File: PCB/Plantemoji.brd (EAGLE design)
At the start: 66.8 x 71 mm, 34 parts, among them IC3 MEGA8-P, Q1 TIP120, Q2 TIP120

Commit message: Putting all the components on the board without routing for now
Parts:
- moved EXTRA_GPIO 253.5 mm to (-5.33, 86.4), turned to 90 degrees
- moved SI1145 199.7 mm to (-9.40, 41.4)
- moved R7 199.5 mm to (-7.37, 35.3)
- moved R6 198.7 mm to (-11.2, 51.8), turned to 90 degrees
- moved Q2 192.6 mm to (-18.0, 92.2), turned to 90 degrees
- moved WATER_LEVEL 191.2 mm to (-19.6, 41.4), turned to 180 degrees
- moved JP2_TX 186.4 mm to (21.1, 92.2)
- moved R1 182.6 mm to (-15.2, 51.8), turned to 90 degrees
- moved DS18B20 178.4 mm to (-28.2, 41.1)
- moved HW-390 170.1 mm to (-37.8, 41.1)
- moved HUMIDIFIER_OUT 152.1 mm to (-20.1, 33.8)
- moved JP2_RX 151.4 mm to (-30.5, 83.8)
- moved R2-0.25W 151.1 mm to (2.79, 79.2), turned to 270 degrees
- moved R3-0.25W 143.4 mm to (3.30, 65.3), turned to 90 degrees
- moved LCD_SCREEN 143.2 mm to (7.37, 96.8), turned to 180 degrees
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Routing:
- net +5V: track 77.3 -> 0.00 mm
- net RESET: track 44.7 -> 0.00 mm
- net N$14: track 12.3 -> 0.00 mm
- net +12V: track 4.57 -> 0.00 mm
- net N$1: track 2.03 -> 0.00 mm

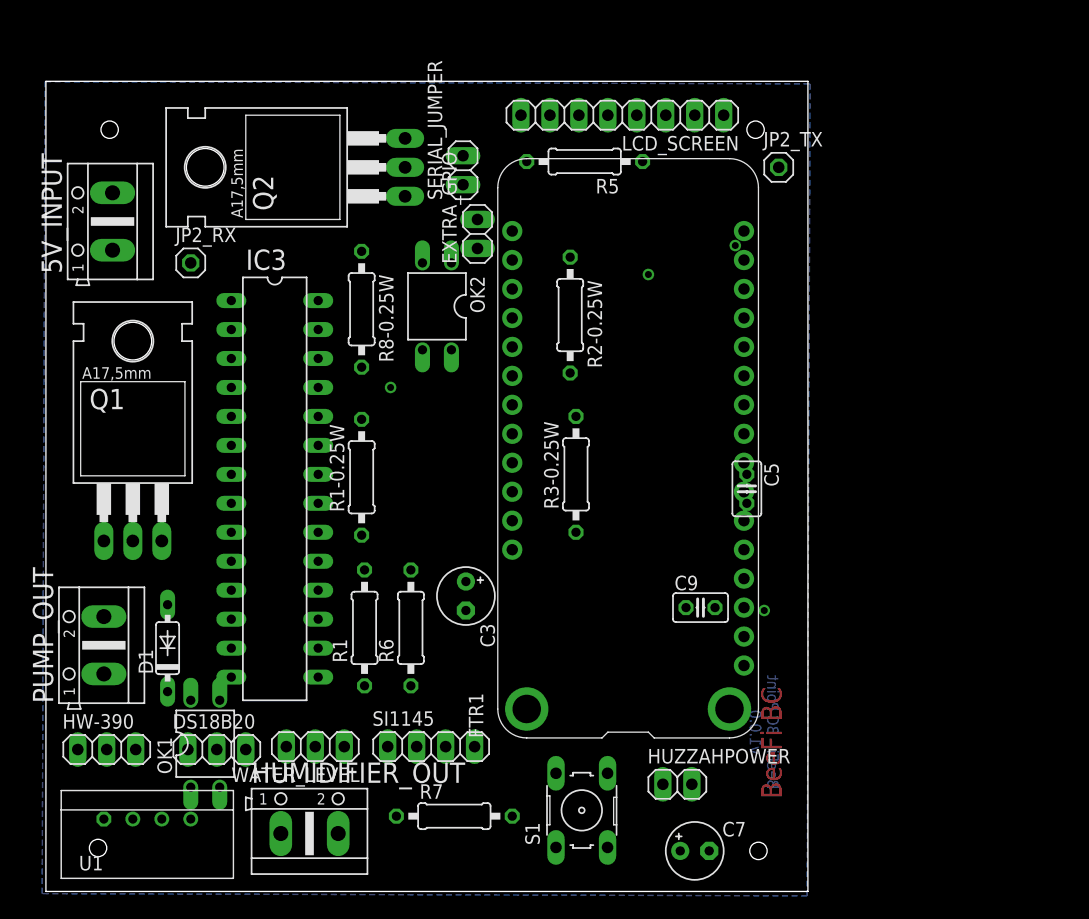
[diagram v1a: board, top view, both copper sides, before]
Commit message: Finish wiring the PCB
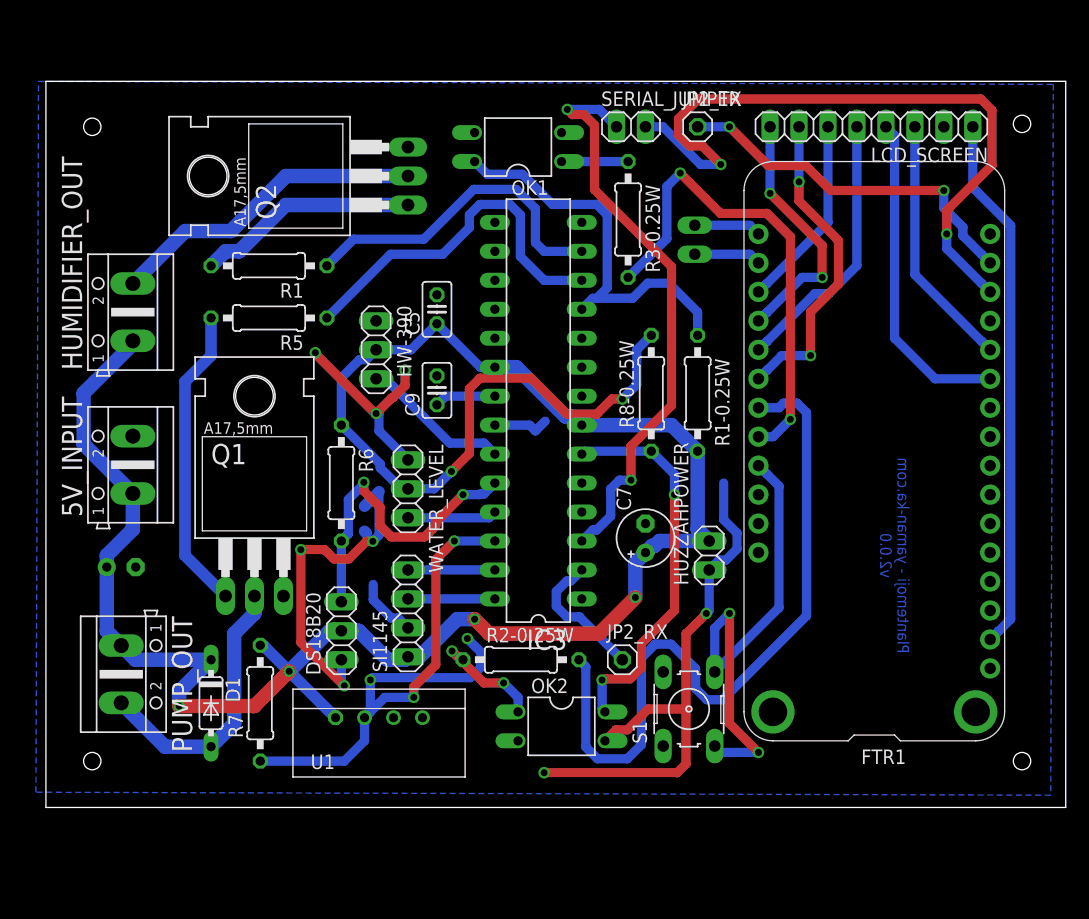
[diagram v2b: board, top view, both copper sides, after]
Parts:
- moved OK1 59.1 mm to (-1.78, 94.0), turned to 90 degrees
- moved JP2_RX 51.4 mm to (7.37, 49.0)
- moved HUMIDIFIER_OUT 48.3 mm to (-35.6, 79.5), turned to 90 degrees
- moved HW-390 42.3 mm to (-14.2, 76.2), turned to 270 degrees
- moved OK2 38.4 mm to (2.03, 43.2), turned to 270 degrees
- moved R1 32.8 mm to (-23.6, 83.6), turned to 180 degrees
- moved C5 31.4 mm to (-8.89, 79.8), turned to 90 degrees
- moved R5 30.9 mm to (-23.6, 79.0)
- moved R2-0.25W 30.5 mm to (-1.52, 49.0), turned to 0 degrees
- moved R1-0.25W 30.4 mm to (14.0, 72.4), turned to 270 degrees
- moved C3 30.3 mm to (-36.6, 57.1), flipped to the bottom, turned to 180 degrees
- moved C9 30.0 mm to (-8.89, 72.6), turned to 90 degrees
- moved C7 27.8 mm to (9.40, 59.7), turned to 90 degrees
- moved R8-0.25W 26.4 mm to (9.91, 72.4), turned to 90 degrees
- moved IC3 24.1 mm to (0.00, 70.9), turned to 90 degrees
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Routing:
- net +5V: track 0.00 -> 205.3 mm, vias 1 -> 6
- net GND: track 0.00 -> 106.4 mm, vias 0 -> 8
- net N$13: track 0.00 -> 65.0 mm
- net N$4: track 0.00 -> 61.9 mm, vias 0 -> 2
- net N$28: track 0.00 -> 52.4 mm, vias 0 -> 4
- net N$3: track 0.00 -> 51.2 mm, vias 0 -> 2
- net 3V3: track 0.00 -> 47.1 mm
- net N$2: track 0.00 -> 44.2 mm, vias 0 -> 2
- net N$16: track 0.00 -> 42.4 mm, vias 0 -> 2
- net N$1: track 0.00 -> 35.5 mm
- net N$11: track 0.00 -> 34.0 mm, vias 0 -> 2
- net N$21: track 0.00 -> 32.0 mm
- net N$18: track 0.00 -> 31.9 mm, vias 0 -> 2
- net N$24: track 0.00 -> 29.1 mm
- net N$6: track 0.00 -> 28.7 mm
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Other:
- board size 66.8 x 71 mm -> 89.4 x 63.7 mm
- board text added: "Plantemoji - yaman-ka.com v2.0.0"
- board text removed: "BeeFi - BC Point v1.0.0"
- board text removed: "BeeFi BC"

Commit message: Final touches before gerber files export
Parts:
- moved JP2_RX 0.72 mm to (6.86, 49.5)
- moved R2-0.25W 0.36 mm to (-1.78, 49.3)
- moved SERIAL_JUMPER 0.25 mm to (8.38, 95.8)
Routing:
- net N$4: track 61.9 -> 36.7 mm
- net +5V: track 205.3 -> 223.5 mm
- net N$28: track 52.4 -> 35.7 mm, vias 4 -> 2
- net N$3: track 51.2 -> 54.1 mm
- net GND: track 106.4 -> 109.2 mm, vias 8 -> 9
- net N$13: track 65.0 -> 67.4 mm
- net N$12: track 10.1 -> 7.82 mm, vias 2 -> 0
- net N$11: track 34.0 -> 36.2 mm
- net N$17: track 12.1 -> 11.3 mm
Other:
- board text added: "Plantemoji - yaman-ka.com CASA - UCL v2.0.0"
- board text removed: "Plantemoji - yaman-ka.com v2.0.0"

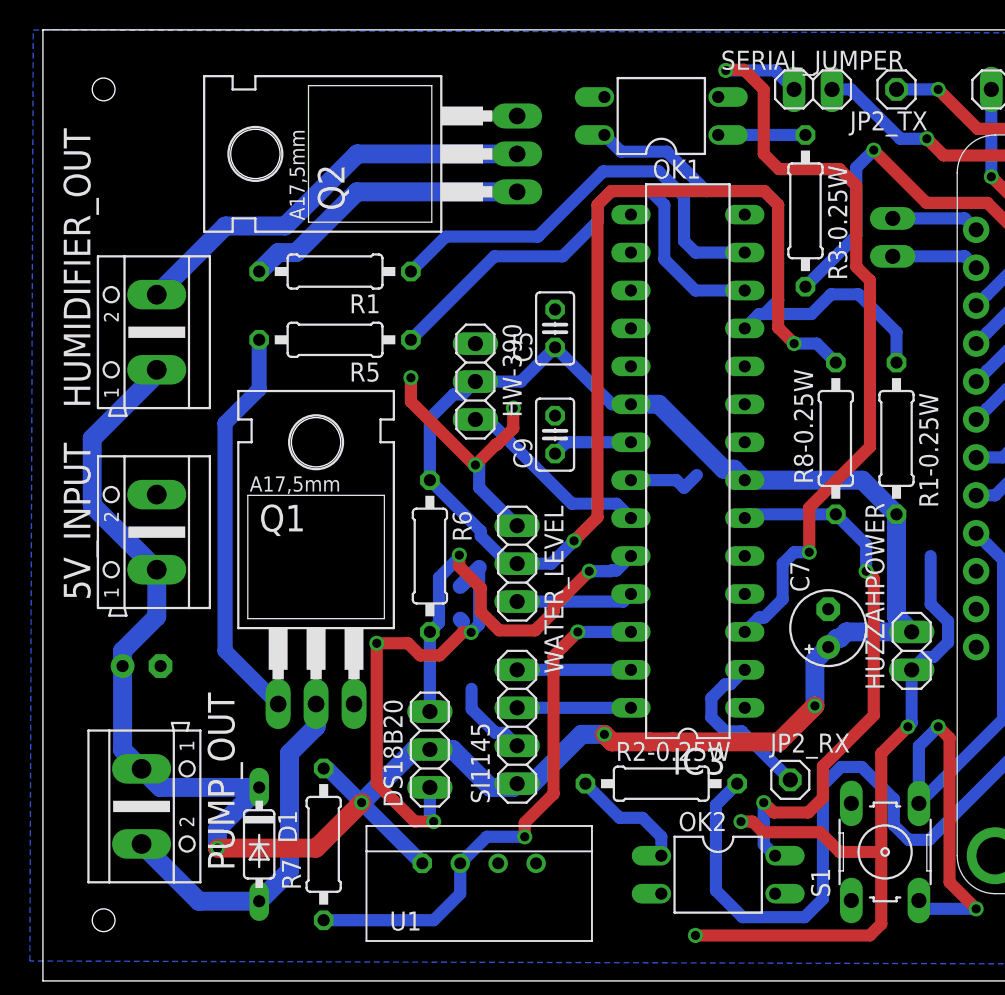
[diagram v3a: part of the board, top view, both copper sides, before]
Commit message: PCB is sent to PCBWay! Gerber files were generated using this tutorial (https://www.pcbway.com/helpcenter/technical_support/Generate_Gerber_files_in_Eagle.html)
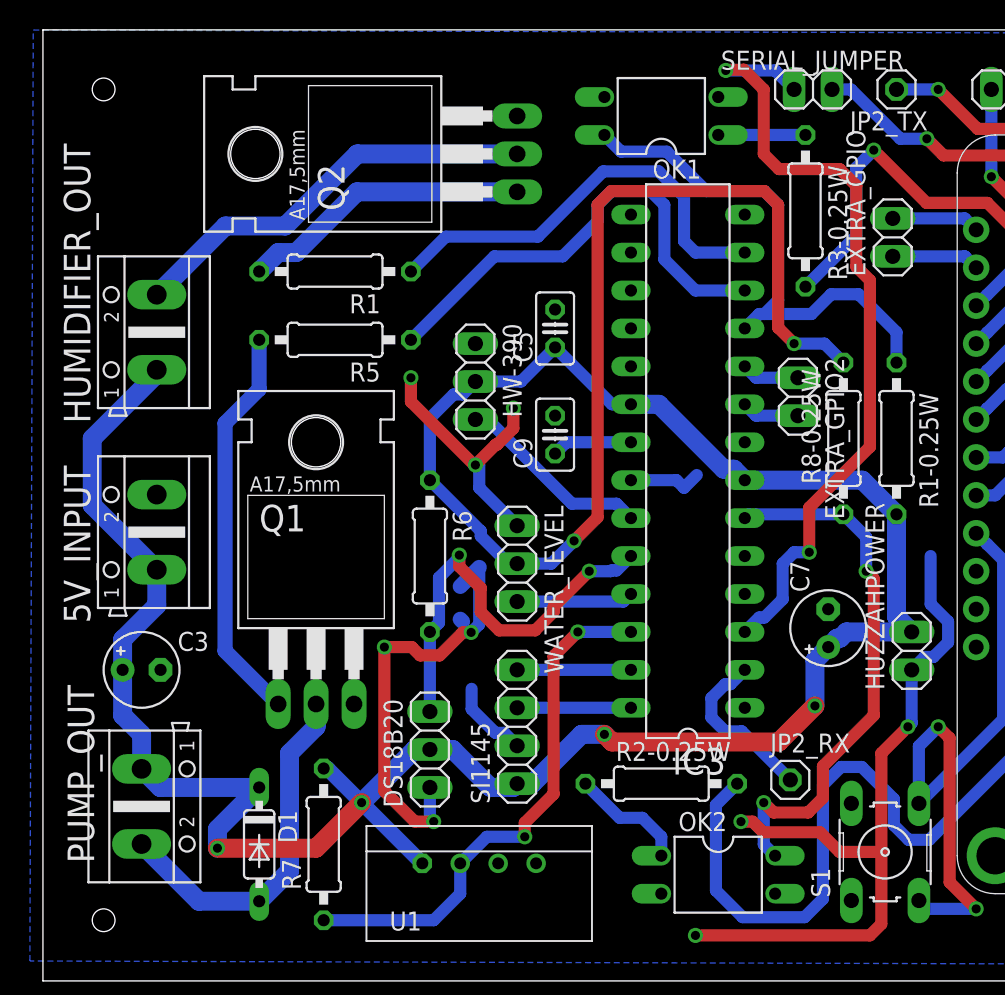
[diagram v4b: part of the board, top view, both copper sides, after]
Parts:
- added EXTRA_GPIO2: (no value), pinhead:1X02
- moved R8-0.25W 0.51 mm to (10.4, 72.4)
- moved C3 0.25 mm to (-36.6, 56.9), flipped to the top, turned to 0 degrees
- flipped EXTRA_GPIO to the top
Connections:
- new net N$33: EXTRA_GPIO2.2, IC3.9
- new net N$34: EXTRA_GPIO2.1, IC3.10
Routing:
- net N$34: track 0.00 -> 3.87 mm
- net N$33: track 0.00 -> 3.87 mm
- net GND: track 109.2 -> 108.1 mm
- net +5V: track 223.5 -> 224.0 mm

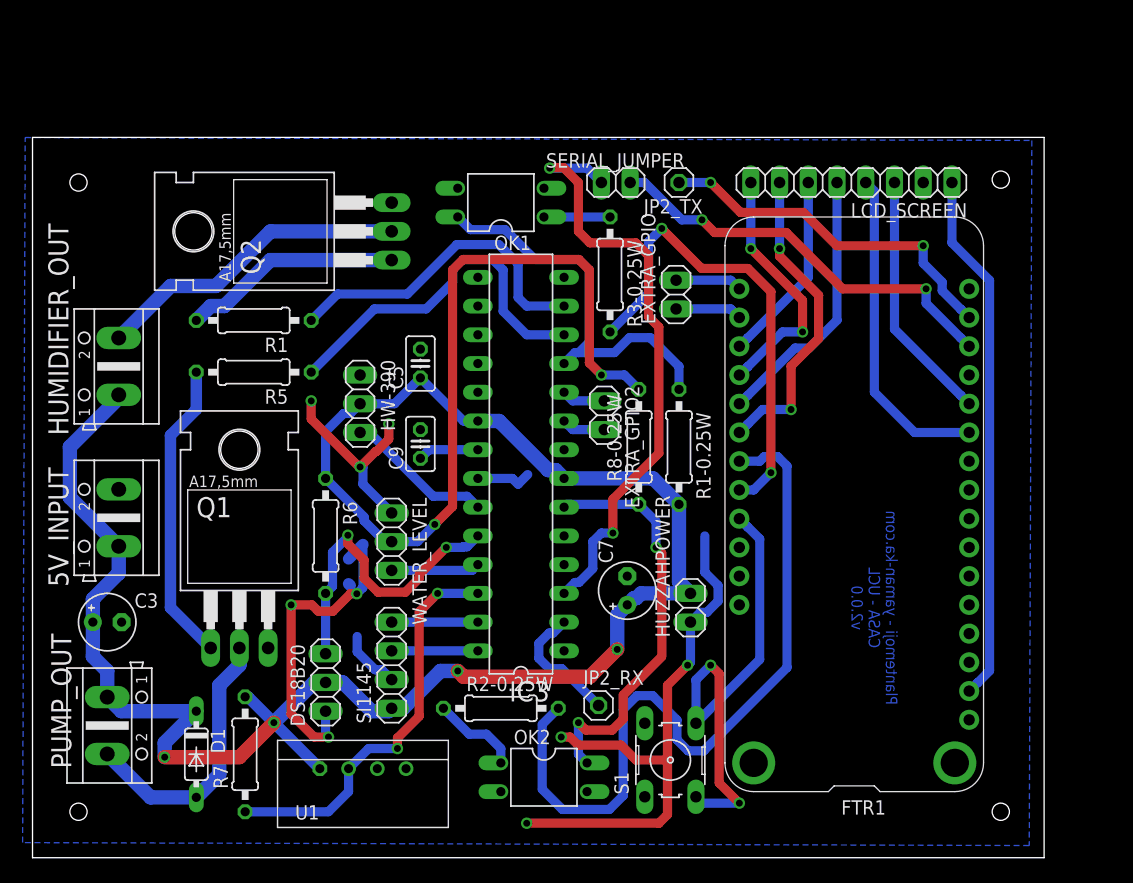
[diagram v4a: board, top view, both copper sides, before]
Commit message: Major update to the PCB: now it's based on ESP32 (FireBeetle) instead of the old ESP8266 (Feather Huzzah)
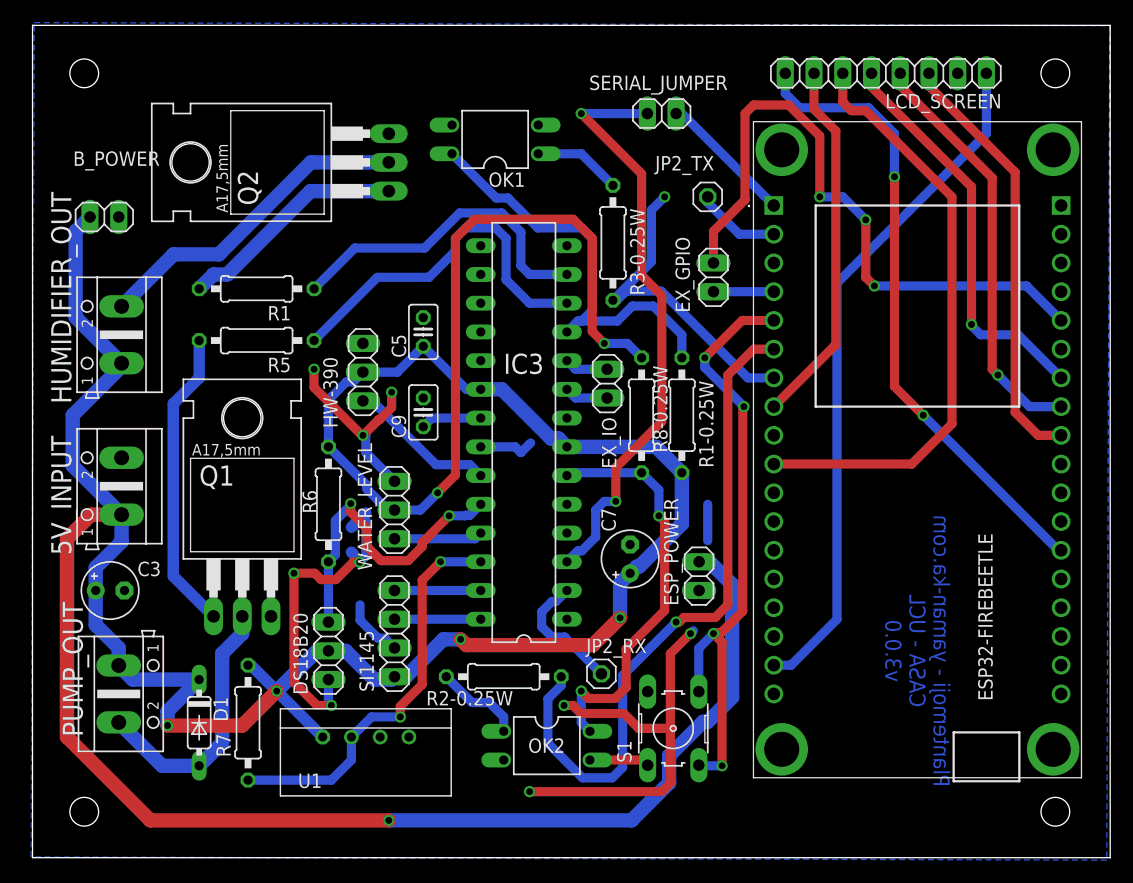
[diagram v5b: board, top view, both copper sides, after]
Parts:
- removed EXTRA_GPIO, EXTRA_GPIO2, HUZZAHPOWER: (no value), pinhead:1X02
- removed FTR1: FEATHER_HUZZAH_ESP8266, adafruit-supplemental-arkane:FEATHER
- added B_POWER, ESP_POWER, EX_GPIO, EX_IO: (no value), pinhead:1X02
- added ESP32-FIREBEETLE: DFR0478, DFR0478:FIREBEETLE_ESP32
- moved LCD_SCREEN 10.1 mm to (32.3, 105.4)
- moved SERIAL_JUMPER 7.33 mm to (12.4, 101.9)
- moved Q2 6.10 mm to (-18.0, 97.5)
- moved OK1 5.61 mm to (-2.29, 99.6)
- moved PUMP_OUT 2.97 mm to (-35.6, 50.5)
- moved JP2_TX 2.84 mm to (16.5, 94.5)
- moved HUMIDIFIER_OUT 2.81 mm to (-35.3, 82.3)
- moved R3-0.25W 2.81 mm to (8.13, 90.4)
- moved WATER_LEVEL 2.81 mm to (-11.2, 66.8)
- moved C7 2.81 mm to (9.65, 62.5)
- moved SI1145 2.81 mm to (-11.2, 55.9)
- moved DS18B20 2.81 mm to (-17.0, 54.4)
- moved 5V_INPUT 2.81 mm to (-35.3, 68.9)
- moved C3 2.81 mm to (-36.3, 59.7)
- moved C5 2.81 mm to (-8.64, 82.5)
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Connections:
- removed net 3V3: FTR1.2, LCD_SCREEN.1
- new net N$35: ESP32-FIREBEETLE.4, EX_GPIO.1
- net +5V: now also B_POWER.2, ESP_POWER.2; no longer HUZZAHPOWER.2
- net GND: now also B_POWER.1, ESP_POWER.1; no longer HUZZAHPOWER.1
- net N$10: now also ESP32-FIREBEETLE.10, LCD_SCREEN.6; no longer FTR1.20, LCD_SCREEN.8
- net N$13: now also ESP32-FIREBEETLE.6; no longer FTR1.23
- net N$16: now also ESP32-FIREBEETLE.7; no longer FTR1.24
- net N$18: now also ESP32-FIREBEETLE.2; no longer FTR1.15
- net N$2: now also ESP32-FIREBEETLE.5; no longer FTR1.25
- net N$31: now also ESP32-FIREBEETLE.31, LCD_SCREEN.8; no longer EXTRA_GPIO.1, FTR1.18
- net N$32: now also ESP32-FIREBEETLE.23, EX_GPIO.2; no longer EXTRA_GPIO.2, FTR1.17
- net N$33: now also EX_IO.2; no longer EXTRA_GPIO2.2
- net N$34: now also EX_IO.1; no longer EXTRA_GPIO2.1
- net N$4: now also ESP32-FIREBEETLE.1; no longer FTR1.14
- net N$5: now also ESP32-FIREBEETLE.17, LCD_SCREEN.1; no longer FTR1.12, LCD_SCREEN.3
- net N$6: now also ESP32-FIREBEETLE.27, LCD_SCREEN.3; no longer FTR1.11, LCD_SCREEN.4
- net N$7: now also ESP32-FIREBEETLE.26, LCD_SCREEN.4; no longer FTR1.21, LCD_SCREEN.5
- net N$8: now also ESP32-FIREBEETLE.8, LCD_SCREEN.7; no longer FTR1.19, LCD_SCREEN.6
- net N$9: now also ESP32-FIREBEETLE.25, LCD_SCREEN.5; no longer FTR1.22, LCD_SCREEN.7
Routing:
- net +5V: track 224.0 -> 340.7 mm, vias 6 -> 7
- net N$32: track 5.90 -> 56.6 mm, vias 0 -> 3
- net N$31: track 5.90 -> 56.0 mm, vias 0 -> 2
- net 3V3: track 47.1 -> 0.00 mm
- net N$5: track 22.3 -> 61.0 mm
- net N$10: track 22.3 -> 53.0 mm, vias 2 -> 0
- net N$4: track 36.7 -> 12.0 mm, vias 2 -> 0
- net N$18: track 31.9 -> 7.51 mm, vias 2 -> 0
- net N$8: track 17.0 -> 32.5 mm
- net N$16: track 42.4 -> 28.8 mm, vias 2 -> 1
- net N$7: track 23.9 -> 37.0 mm, vias 0 -> 1
- net N$2: track 44.2 -> 54.5 mm, vias 2 -> 4
- net N$6: track 28.7 -> 38.0 mm
- net N$9: track 27.9 -> 35.8 mm, vias 2 -> 1
- net N$13: track 67.4 -> 60.0 mm, vias 0 -> 1
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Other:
- board size 89.4 x 63.7 mm -> 95.3 x 73.6 mm
- board text added: "Plantemoji - yaman-ka.com CASA - UCL v3.0.0"
- board text removed: "Plantemoji - yaman-ka.com CASA - UCL v2.0.0"
